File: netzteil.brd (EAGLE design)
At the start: 100 x 80 mm, 43 parts

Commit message: version2
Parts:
- moved U$5 13.9 mm to (27.9, 47.6), turned to 0 degrees
- moved U$7 13.3 mm to (26.7, 52.1), turned to 180 degrees
- moved U$3 13.0 mm to (43.2, 52.1), turned to 0 degrees
- moved C1 12.7 mm to (14.0, 57.8)
- moved D3 12.6 mm to (61.0, 34.3)
- moved C6 10.2 mm to (53.3, 57.8)
- moved C7 10.2 mm to (55.9, 57.8)
- moved C3 10.2 mm to (11.4, 57.8)
- moved C5 10.2 mm to (50.8, 57.8)
- moved C16 10.2 mm to (62.2, 57.1)
- moved U$1 8.98 mm to (50.8, 34.3), turned to 180 degrees
- moved R3 7.73 mm to (11.4, 44.5), turned to 90 degrees
- moved C2 7.65 mm to (16.5, 57.8)
- moved C9 7.18 mm to (15.9, 37.5)
- moved R2 6.35 mm to (66.0, 45.7), turned to 90 degrees
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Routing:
- net VINN: track 65.1 -> 0.00 mm
- net +24V: track 62.1 -> 0.00 mm
- net N$3: track 66.4 -> 13.8 mm
- net N$12: track 50.4 -> 0.00 mm
- net SW1: track 36.2 -> 0.96 mm
- net SNSP: track 50.3 -> 20.3 mm, vias 2 -> 0
- net +12V: track 29.8 -> 0.00 mm, vias 2 -> 0
- net N$4: track 47.0 -> 19.8 mm
- net GND: track 51.4 -> 28.2 mm
- net ISP: track 22.3 -> 0.00 mm, vias 2 -> 0

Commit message: version3
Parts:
- C10, C14, C15, C9: device resistor:C0603K -> resistor:C0805K
- moved C10 77.3 mm to (19.1, 38.7), turned to 90 degrees
- moved R2 55.9 mm to (10.2, 44.5), turned to 270 degrees
- moved C16 54.0 mm to (8.26, 57.1)
- moved C3 48.9 mm to (60.3, 57.8)
- moved R3 47.0 mm to (58.4, 45.7)
- moved C1 43.8 mm to (57.8, 57.8)
- moved C2 38.7 mm to (55.2, 57.8)
- moved C9 38.1 mm to (54.0, 36.2), turned to 0 degrees
- moved C5 36.8 mm to (14.0, 57.8)
- moved C6 36.8 mm to (16.5, 57.8)
- moved C7 36.8 mm to (19.1, 57.8)
- moved R4 35.6 mm to (52.7, 42.5)
- moved C4 33.7 mm to (52.7, 57.8)
- moved U$6 31.8 mm to (50.8, 50.2), turned to 0 degrees
- moved U$2 31.7 mm to (19.1, 52.1), turned to 180 degrees
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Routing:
- net VINN: track 0.00 -> 51.8 mm
- net +24V: track 0.00 -> 48.2 mm
- net +5V: track 0.00 -> 43.2 mm
- net N$12: track 0.00 -> 39.4 mm
- net N$3: track 13.8 -> 50.8 mm
- net GND: track 28.2 -> 64.4 mm, vias 2 -> 3
- net N$11: track 0.00 -> 33.2 mm
- net N$8: track 0.00 -> 31.2 mm, vias 0 -> 2
- net SNSP: track 20.3 -> 48.6 mm, vias 0 -> 2
- net N$6: track 0.00 -> 27.9 mm, vias 0 -> 2
- net SW1: track 0.96 -> 25.9 mm
- net ISP: track 0.00 -> 21.7 mm
- net N$4: track 19.8 -> 40.9 mm
- net +12V: track 0.00 -> 21.0 mm
- net SW2: track 0.00 -> 20.2 mm
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
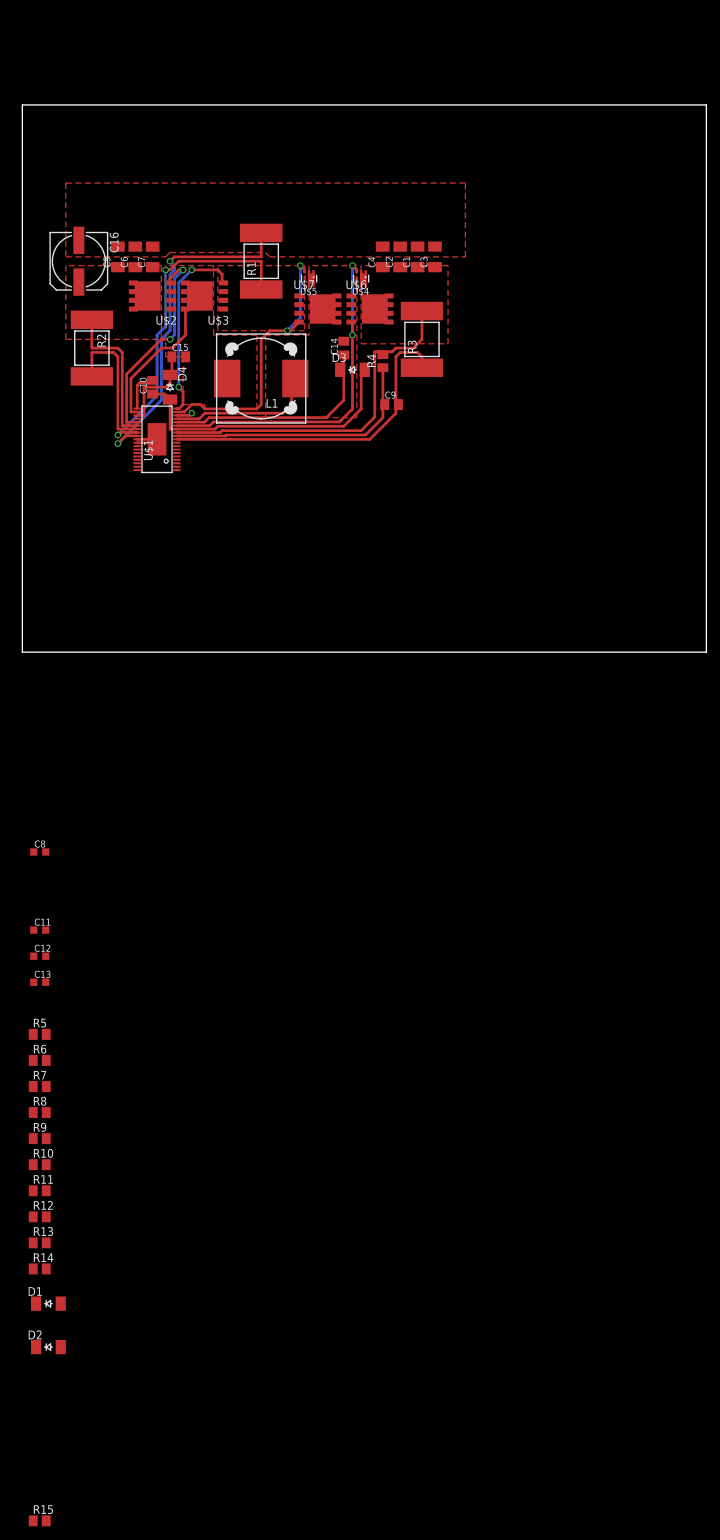
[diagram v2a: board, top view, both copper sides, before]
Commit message: an platinenbelichter gesendet, hohlstecker verpolt
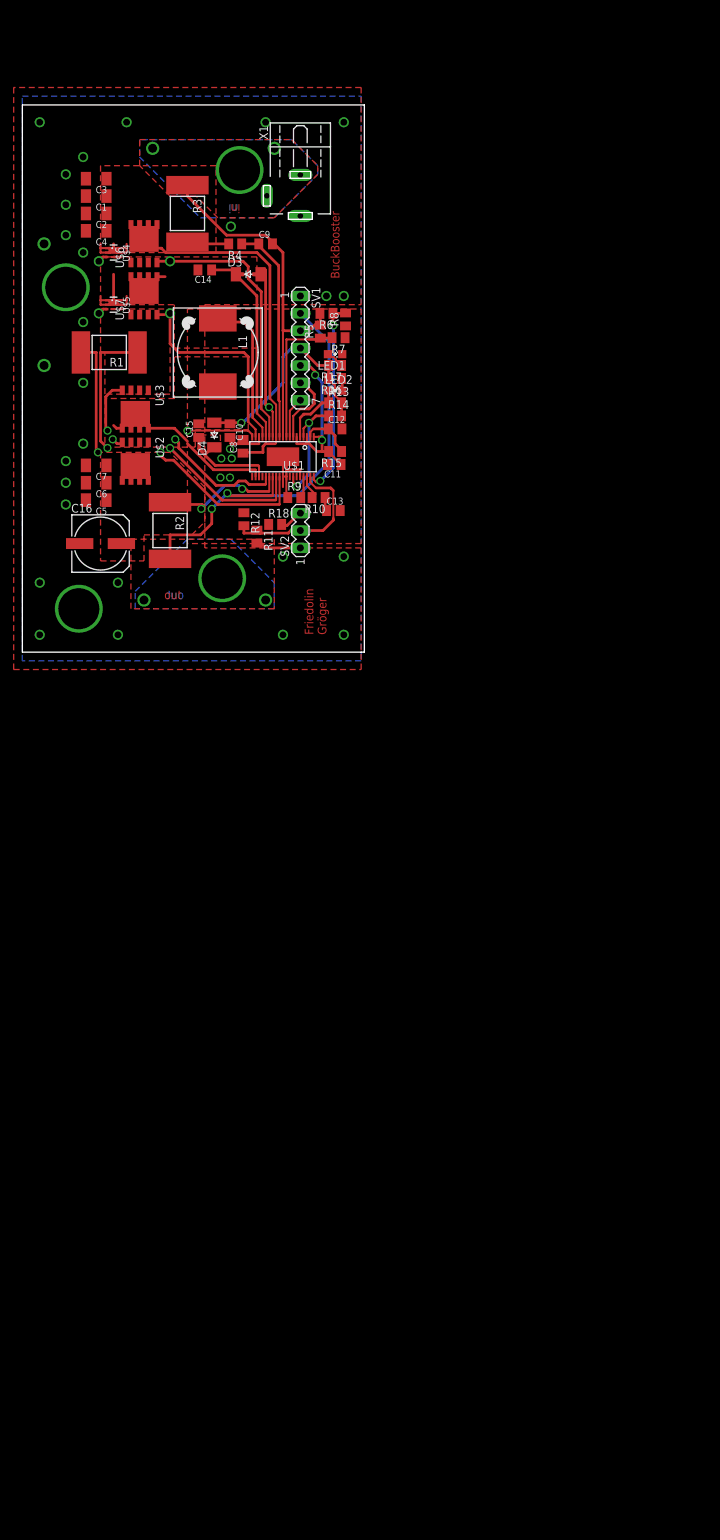
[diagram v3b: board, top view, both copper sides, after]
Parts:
- removed D1, D2: CGRM4001-G, diode:SOD-123_MINI-SMA
- added LED1, LED2: (no value), led:SML0805
- added R16, R17: 51, resistor:M0805
- added R18: 8k06, resistor:M0805
- added SV1: (no value), con-lstb:MA07-1
- added SV2: (no value), con-lstb:MA03-1
- added X1: NEB21R, con-lumberg:NEB21R
- C11, C12, C13, C8: device resistor:C0603K -> resistor:C0805K
- moved R15 162.2 mm to (45.7, 29.3), turned to 180 degrees
- moved R14 132.0 mm to (45.7, 34.5)
- moved R13 130.2 mm to (45.7, 36.4)
- moved R8 124.3 mm to (47.2, 48.6), turned to 90 degrees
- moved R7 117.9 mm to (46.2, 46.0), turned to 180 degrees
- moved R6 117.0 mm to (44.5, 49.5), turned to 180 degrees
- moved R5 110.6 mm to (43.6, 46.9), turned to 90 degrees
- moved R12 106.3 mm to (32.4, 19.4), turned to 270 degrees
- moved R10 105.7 mm to (43.3, 22.6), turned to 180 degrees
- moved R9 100.8 mm to (39.8, 22.6)
- moved R11 100.8 mm to (34.3, 16.9), turned to 270 degrees
- moved C12 88.4 mm to (45.7, 32.6)
- moved C13 81.2 mm to (45.5, 20.7)
- moved C11 80.5 mm to (45.6, 27.4), turned to 180 degrees
- moved C8 66.3 mm to (32.3, 30.1), turned to 90 degrees
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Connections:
- net N$11 renamed BST1
- net N$3 renamed TG1
- net N$4 renamed BG1
- net N$6 renamed BG2
- net N$7 renamed BST2
- net N$8 renamed TG2
- new net N$1: U$1.28
- new net N$2: SV1.6, U$1.7
- new net N$3: SV1.7, U$1.8
- new net N$4: LED1.A, R17.1
- new net N$5: LED2.A, R16.1
- new net N$6: R18.2, SV2.3
- net +12V: now also SV1.2, SV2.1
- net +24V: now also SV1.3, X1.3
- net +5V: now also R16.2, R17.2, SV1.4
- net GND: now also LED1.C, R18.1, SV1.1, X1.1; no longer U$1.28
- net N$17: now also SV2.2
- net N$20: now also LED2.C
- net N$25: now also SV1.5
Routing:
- net +12V: track 21.0 -> 72.9 mm, vias 0 -> 5
- net GND: track 64.4 -> 20.5 mm, vias 3 -> 35
- net N$1: track 0.00 -> 41.5 mm, vias 0 -> 2
- net N$14: track 0.00 -> 28.8 mm, vias 0 -> 2
- net N$25: track 0.00 -> 26.4 mm, vias 0 -> 2
- net N$17: track 0.00 -> 24.6 mm
- net N$13: track 0.00 -> 21.0 mm
- net +5V: track 43.2 -> 62.3 mm, vias 0 -> 2
- net N$18: track 0.00 -> 17.3 mm, vias 0 -> 2
- net VINN: track 51.8 -> 68.6 mm
- net SW1: track 25.9 -> 38.2 mm
- net TG2: track 31.2 -> 19.9 mm
- net N$2: track 0.00 -> 11.0 mm
- net BG2: track 27.9 -> 17.9 mm
- net N$20: track 0.00 -> 9.68 mm
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- added copper zone on layer 1, net +12V
- added copper zone on layer 16, net +12V
- added copper zone on layer 1, net +24V
- added copper zone on layer 16, net +24V
- added copper zone on layer 1, net BST2
- added copper zone on layer 16, net GND
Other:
- board size 100 x 80 mm -> 50 x 80 mm
- board text added: "BuckBooster"
- board text added: "Friedolin Gröger"
- board text added: "in"
- board text added: "out"

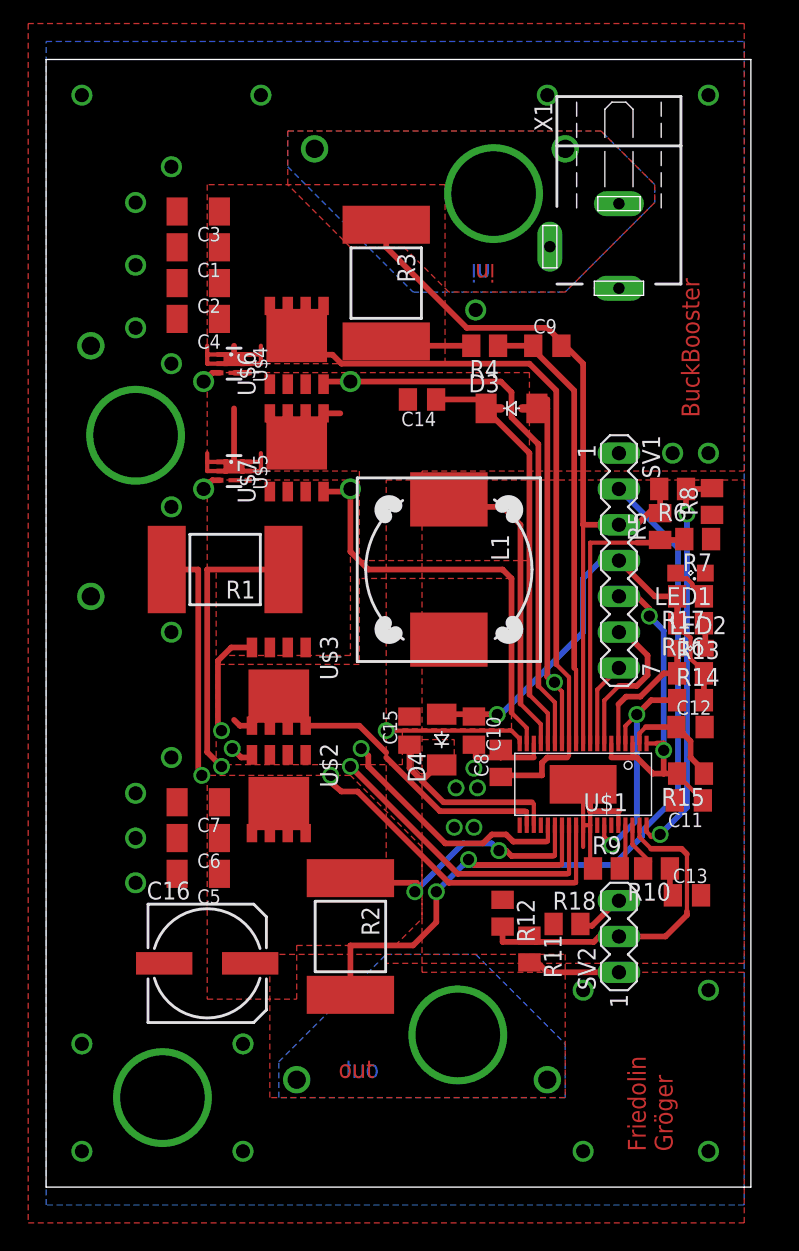
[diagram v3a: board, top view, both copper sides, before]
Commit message: platine V1 gefertigt
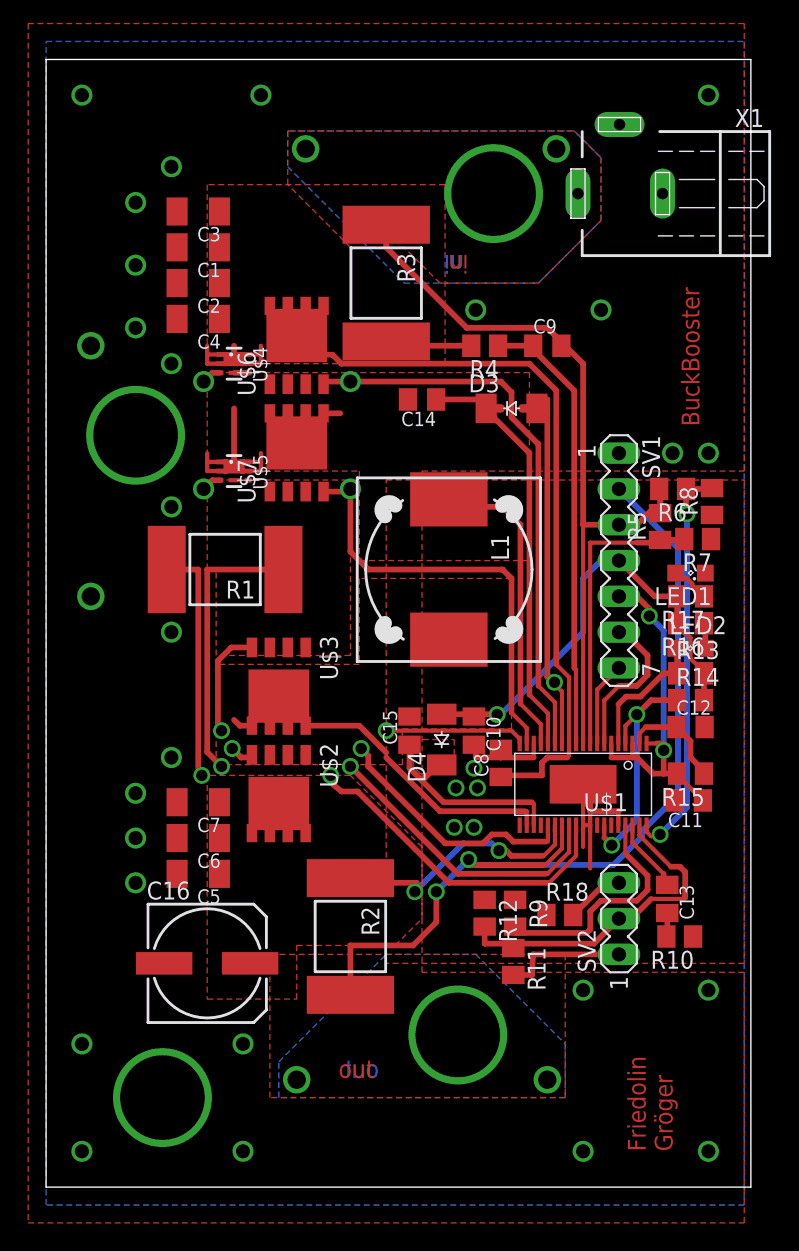
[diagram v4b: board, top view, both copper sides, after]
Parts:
- moved R9 7.21 mm to (33.3, 19.4), turned to 270 degrees
- moved R10 5.10 mm to (45.0, 17.8)
- moved X1 4.49 mm to (45.1, 70.5), turned to 90 degrees
- moved R11 1.45 mm to (33.1, 16.0)
- moved C13 1.42 mm to (44.1, 20.4), turned to 270 degrees
- moved R12 1.27 mm to (31.1, 19.4)
- moved SV2 1.27 mm to (40.6, 19.1)
- moved R18 0.81 mm to (36.4, 19.3)
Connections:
- removed net N$21: C13.1, R10.1
- removed net N$23: R10.2, U$1.36
- new net N$7: C13.2, R10.2
- new net N$8: C13.1, U$1.36
- net +24V: now also X1.1; no longer X1.3
- net GND: now also R10.1, X1.2, X1.3; no longer C13.2, X1.1
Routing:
- net N$24: track 3.23 -> 17.0 mm
- net N$8: track 0.00 -> 5.30 mm
- net N$23: track 3.73 -> 0.00 mm
- net N$21: track 2.11 -> 0.00 mm
- net N$7: track 0.00 -> 1.69 mm
- net +12V: track 72.9 -> 74.4 mm
- net N$1: track 41.5 -> 40.4 mm
- net SNSP: track 41.9 -> 41.0 mm
- net N$17: track 24.6 -> 24.0 mm
- net N$6: track 3.59 -> 4.19 mm
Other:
- outline, holes or cut-outs redrawn

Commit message: version v1 bestückt
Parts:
- C13: value 22n -> 5n
- R1: value 0,004 -> 0,005
- R10: value 5k1 -> 12k
- R11: value 73k2 -> 470k
- R12: value 8k06 -> 30k
- R16: value 51 -> 0
- R17: value 51 -> 330
- R18: value 8k06 -> 10k
- R2: value 0,009 -> 0,01
- R3: value 0,003 -> 0,004
- R5: value 866k -> 470k
- R6: value 1M -> 470k
- R7: value 576k -> 100k
- R8: value 57k6 -> 56k
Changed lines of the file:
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@@
 <setting verticaltext="up"/>
 </settings>
-<grid distance="1.27" unitdist="mm" unit="mm" style="lines" multiple="1" display="yes" altdistance="5" altunitdist="mil" altunit="mil"/>
+<grid distance="1" unitdist="mm" unit="mm" style="lines" multiple="1" display="yes" altdistance="5" altunitdist="mil" altunit="mil"/>
 <layers>
 <layer number="1" name="Top" color="4" fill="1" visible="yes" active="yes"/>
-<layer number="16" name="Bottom" color="1" fill="1" visible="yes" active="yes"/>
+<layer number="16" name="Bottom" color="1" fill="1" visible="no" active="yes"/>
 <layer number="17" name="Pads" color="2" fill="1" visible="yes" active="yes"/>
 <layer number="18" name="Vias" color="2" fill="1" visible="yes" active="yes"/>
@@
 <layer number="25" name="tNames" color="7" fill="1" visible="no" active="yes"/>
 <layer number="26" name="bNames" color="7" fill="1" visible="no" active="yes"/>
-<layer number="27" name="tValues" color="7" fill="1" visible="no" active="yes"/>
-<layer number="28" name="bValues" color="7" fill="1" visible="no" active="yes"/>
+<layer number="27" name="tValues" color="7" fill="1" visible="yes" active="yes"/>
+<layer number="28" name="bValues" color="7" fill="1" visible="yes" active="yes"/>
 <layer number="29" name="tStop" color="7" fill="3" visible="no" active="yes"/>
 <layer number="30" name="bStop" color="7" fill="6" visible="no" active="yes"/>
@@
 <element name="U$4" library="teile" package="SC70-6L" value="SIA440DJ" x="13.335" y="58.42" rot="R270"/>
 <element name="U$5" library="teile" package="SC70-6L" value="SIA440DJ" x="13.335" y="50.8" rot="R270"/>
-<element name="R1" library="resistor-shunt" package="BVS" value="0,004" x="12.7" y="43.815" rot="R180">
+<element name="R1" library="resistor-shunt" package="BVS" value="0,005" x="12.7" y="43.815" rot="R180">
 <attribute name="OC_NEWARK" value="unknown" x="12.7" y="43.815" size="1.778" layer="27" rot="R180" display="off"/>
 <attribute name="MPN" value="" x="12.7" y="43.815" size="1.778" layer="27" rot="R180" display="off"/>
@@
 <attribute name="OC_FARNELL" value="unknown" x="12.7" y="43.815" size="1.778" layer="27" rot="R180" display="off"/>
 </element>
-<element name="R2" library="resistor-shunt" package="BVS" value="0,009" x="21.59" y="17.78" rot="R270">
+<element name="R2" library="resistor-shunt" package="BVS" value="0,01" x="21.59" y="17.78" rot="R270">
 <attribute name="OC_NEWARK" value="unknown" x="21.59" y="17.78" size="1.778" layer="27" rot="R270" display="off"/>
 <attribute name="MPN" value="" x="21.59" y="17.78" size="1.778" layer="27" rot="R270" display="off"/>
@@
 <attribute name="OC_FARNELL" value="unknown" x="21.59" y="17.78" size="1.778" layer="27" rot="R270" display="off"/>
 </element>
-<element name="R3" library="resistor-shunt" package="BVS" value="0,003" x="24.13" y="64.135" rot="R270">
+<element name="R3" library="resistor-shunt" package="BVS" value="0,004" x="24.13" y="64.135" rot="R270">
 <attribute name="OC_NEWARK" value="unknown" x="24.13" y="64.135" size="1.778" layer="27" rot="R270" display="off"/>
 <attribute name="MPN" value="" x="24.13" y="64.135" size="1.778" layer="27" rot="R270" display="off"/>
@@
 <element name="C11" library="resistor" package="C0805K" value="100n" x="45.593" y="27.432" rot="R180"/>
 <element name="C12" library="resistor" package="C0805K" value="33n" x="45.72" y="32.639"/>
-<element name="C13" library="resistor" package="C0805K" value="22n" x="44.069" y="20.447" rot="R270"/>
+<element name="C13" library="resistor" package="C0805K" value="5n" x="44.069" y="20.447" rot="R270"/>
 <element name="R4" library="resistor" package="M0805" value="51" x="31.115" y="59.69" rot="R180"/>
-<element name="R5" library="resistor" package="M0805" value="866k" x="43.561" y="46.863" rot="R90"/>
-<element name="R6" library="resistor" package="M0805" value="1M" x="44.45" y="49.53" rot="R180"/>
-<element name="R7" library="resistor" package="M0805" value="576k" x="46.228" y="45.974" rot="R180"/>
-<element name="R8" library="resistor" package="M0805" value="57k6" x="47.244" y="48.641" rot="R90"/>
+<element name="R5" library="resistor" package="M0805" value="470k" x="43.561" y="46.863" rot="R90"/>
+<element name="R6" library="resistor" package="M0805" value="470k" x="44.45" y="49.53" rot="R180"/>
+<element name="R7" library="resistor" package="M0805" value="100k" x="46.228" y="45.974" rot="R180"/>
+<element name="R8" library="resistor" package="M0805" value="56k" x="47.244" y="48.641" rot="R90"/>
 <element name="R9" library="resistor" package="M0805" value="84k5" x="33.274" y="19.431" rot="R270"/>
-<element name="R10" library="resistor" package="M0805" value="5k1" x="44.958" y="17.78" rot="R180"/>
-<element name="R11" library="resistor" package="M0805" value="73k2" x="33.147" y="16.002" rot="R270"/>
-<element name="R12" library="resistor" package="M0805" value="8k06" x="31.115" y="19.431" rot="R270"/>
+<element name="R10" library="resistor" package="M0805" value="12k" x="44.958" y="17.78" rot="R180"/>
+<element name="R11" library="resistor" package="M0805" value="470k" x="33.147" y="16.002" rot="R270"/>
+<element name="R12" library="resistor" package="M0805" value="30k" x="31.115" y="19.431" rot="R270"/>
 <element name="R13" library="resistor" package="M0805" value="200k" x="45.72" y="36.449"/>
 <element name="R14" library="resistor" package="M0805" value="100k" x="45.72" y="34.544"/>
@@
 <element name="LED1" library="led" package="SML0805" value="" x="45.72" y="43.561" rot="R180"/>
 <element name="LED2" library="led" package="SML0805" value="" x="45.72" y="38.227"/>
-<element name="R16" library="resistor" package="M0805" value="51" x="45.72" y="40.005" rot="R180"/>
-<element name="R17" library="resistor" package="M0805" value="51" x="45.72" y="41.91" rot="R180"/>
+<element name="R16" library="resistor" package="M0805" value="0" x="45.72" y="40.005" rot="R180"/>
+<element name="R17" library="resistor" package="M0805" value="330" x="45.72" y="41.91" rot="R180"/>
 <element name="X1" library="con-lumberg" package="NEB21R" value="NEB21R" x="45.085" y="70.485" rot="R90">
 <attribute name="OC_NEWARK" value="97K6458" x="45.085" y="70.485" size="1.778" layer="27" rot="R90" display="off"/>
@@
 <attribute name="OC_FARNELL" value="1217037" x="45.085" y="70.485" size="1.778" layer="27" rot="R90" display="off"/>
 </element>
-<element name="R18" library="resistor" package="M0805" value="8k06" x="36.449" y="19.304"/>
+<element name="R18" library="resistor" package="M0805" value="10k" x="36.449" y="19.304"/>
 </elements>
 <signals>
